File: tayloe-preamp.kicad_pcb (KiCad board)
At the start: 2 copper layers, 39 x 21 mm, 14 parts, among them J1 PCB_SMA_EDGE, J2 PCB_SMA_EDGE, J3 Conn_01x01_Female, Q1 2N2222, T1 T37_XFRM

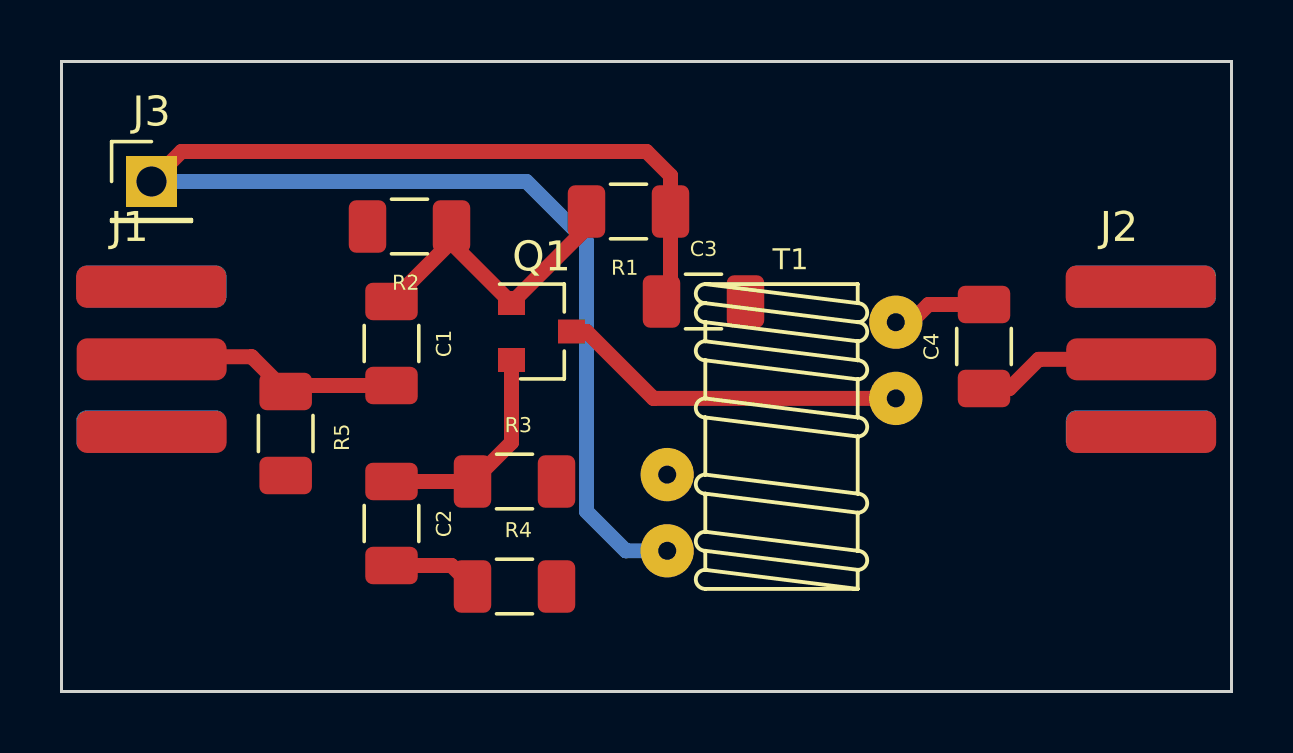
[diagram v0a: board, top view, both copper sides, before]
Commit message: changed to inductor
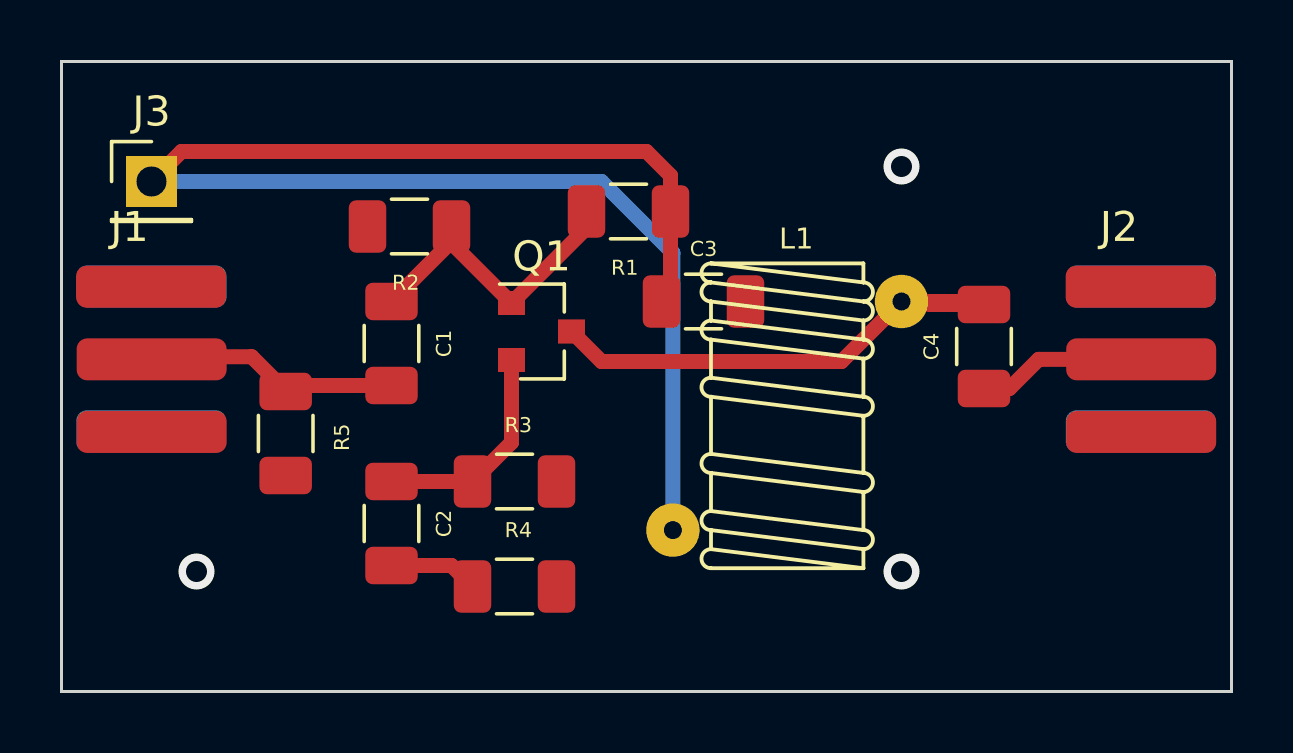
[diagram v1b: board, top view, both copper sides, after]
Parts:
- removed T1: T37_XFRM, Xenir:T37 Transformer
- added L1: Inductor, Xenir:T37_Inductor, F.Cu at (168.2, 87.8)
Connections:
- Q1 pad 3: Net-(Q1-Pad3) -> Net-(C4-Pad2)
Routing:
- net Net-(C4-Pad2): track 3.18 -> 16.9 mm
- net Net-(Q1-Pad3): track 11.7 -> 0.00 mm
- net GND: vias 0 -> 3

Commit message: gg
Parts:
- L1: value Inductor -> T37-43 10T

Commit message: gg
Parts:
- moved C4 3.91 mm to (171.4, 96.2), turned to 180 degrees
- moved R5 2.50 mm to (153.9, 93.0)
- moved R3 2.50 mm to (161.2, 93.1)
- moved J2 2.48 mm to (177.5, 87.8)
- moved R4 2.24 mm to (160.2, 96.1)
- moved C2 0.50 mm to (157.2, 97.9)
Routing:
- net Net-(C4-Pad2): track 16.9 -> 13.5 mm
- net Net-(C1-Pad2): track 8.39 -> 9.54 mm
- net Net-(C2-Pad2): track 2.99 -> 4.03 mm
- net Net-(C2-Pad1): track 7.29 -> 7.95 mm
- net Net-(C4-Pad1): track 5.65 -> 5.15 mm
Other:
- board size 39 x 21 mm -> 36.5 x 19 mm
